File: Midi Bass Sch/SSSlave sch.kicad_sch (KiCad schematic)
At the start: 4 parts

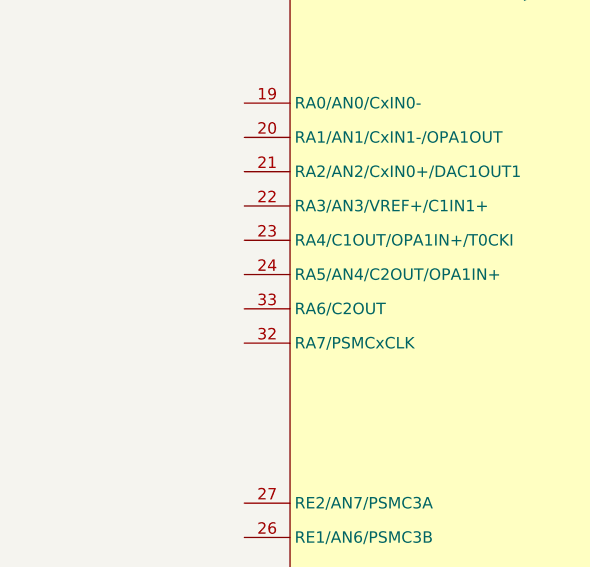
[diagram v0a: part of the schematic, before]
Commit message: updated schematic to include test points for pics
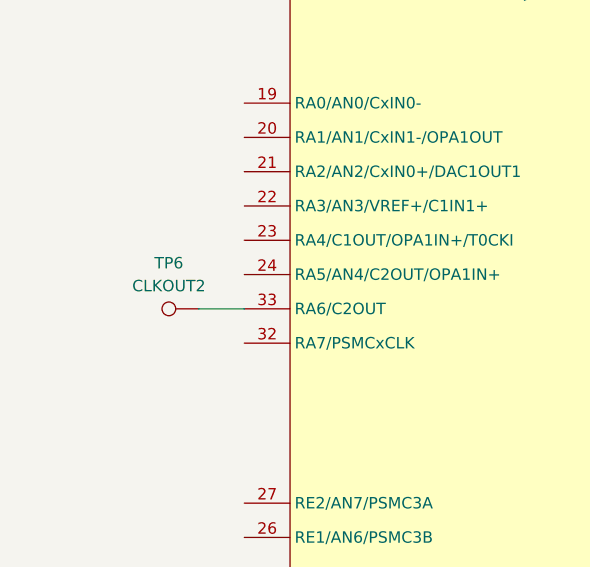
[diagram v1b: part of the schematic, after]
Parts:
- added TP6: CLKOUT2, symbol Connector:TestPoint
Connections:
- net at U3.33 (RA6/C2OUT): now also TP6.1
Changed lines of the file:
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@@
+	(wire
+		(pts
+			(xy 71.12 72.39) (xy 76.2 72.39)
+		)
+		(stroke
+			(width 0)
+			(type default)
+		)
+	)
 	(wire
 		(pts
@@
 					(unit 1)
 				)
+			)
+		)
+	)
+	(symbol
+		(lib_id "Connector:TestPoint")
+		(at 71.12 72.39 90)
+		(unit 1)
+		(exclude_from_sim no)
+		(in_bom yes)
+		(on_board yes)
+		(dnp no)
+		(fields_autoplaced yes)
+		(property "Reference" "TP6"
+			(at 67.818 67.31 90)
+			(effects
+				(font
+					(size 1.27 1.27)
+				)
+			)
+		)
+		(property "Value" "CLKOUT2"
+			(at 67.818 69.85 90)
+			(effects
+				(font
+					(size 1.27 1.27)
+				)
+			)
+		)
+		(property "Footprint" ""
+			(at 71.12 67.31 0)
+			(effects
+				(font
+					(size 1.27 1.27)
+				)
+				(hide yes)
+			)
+		)
+		(property "Datasheet" "~"
+			(at 71.12 67.31 0)
+			(effects
+				(font
+					(size 1.27 1.27)
+				)
+				(hide yes)
+			)
+		)
+		(property "Description" "test point"
+			(at 71.12 72.39 0)
+			(effects
+				(font
+					(size 1.27 1.27)
+				)
+				(hide yes)
+			)
+		)
+		(pin "1"
+		)
+		(instances
+			(project "Midi Bass Sch"
+				(path "/06818073-fb22-48ee-acc5-6dedd827034e/673444b1-2638-4f61-b545-e7cdf999c0e0"
+					(reference "TP6")
+					(unit 1)
+				)

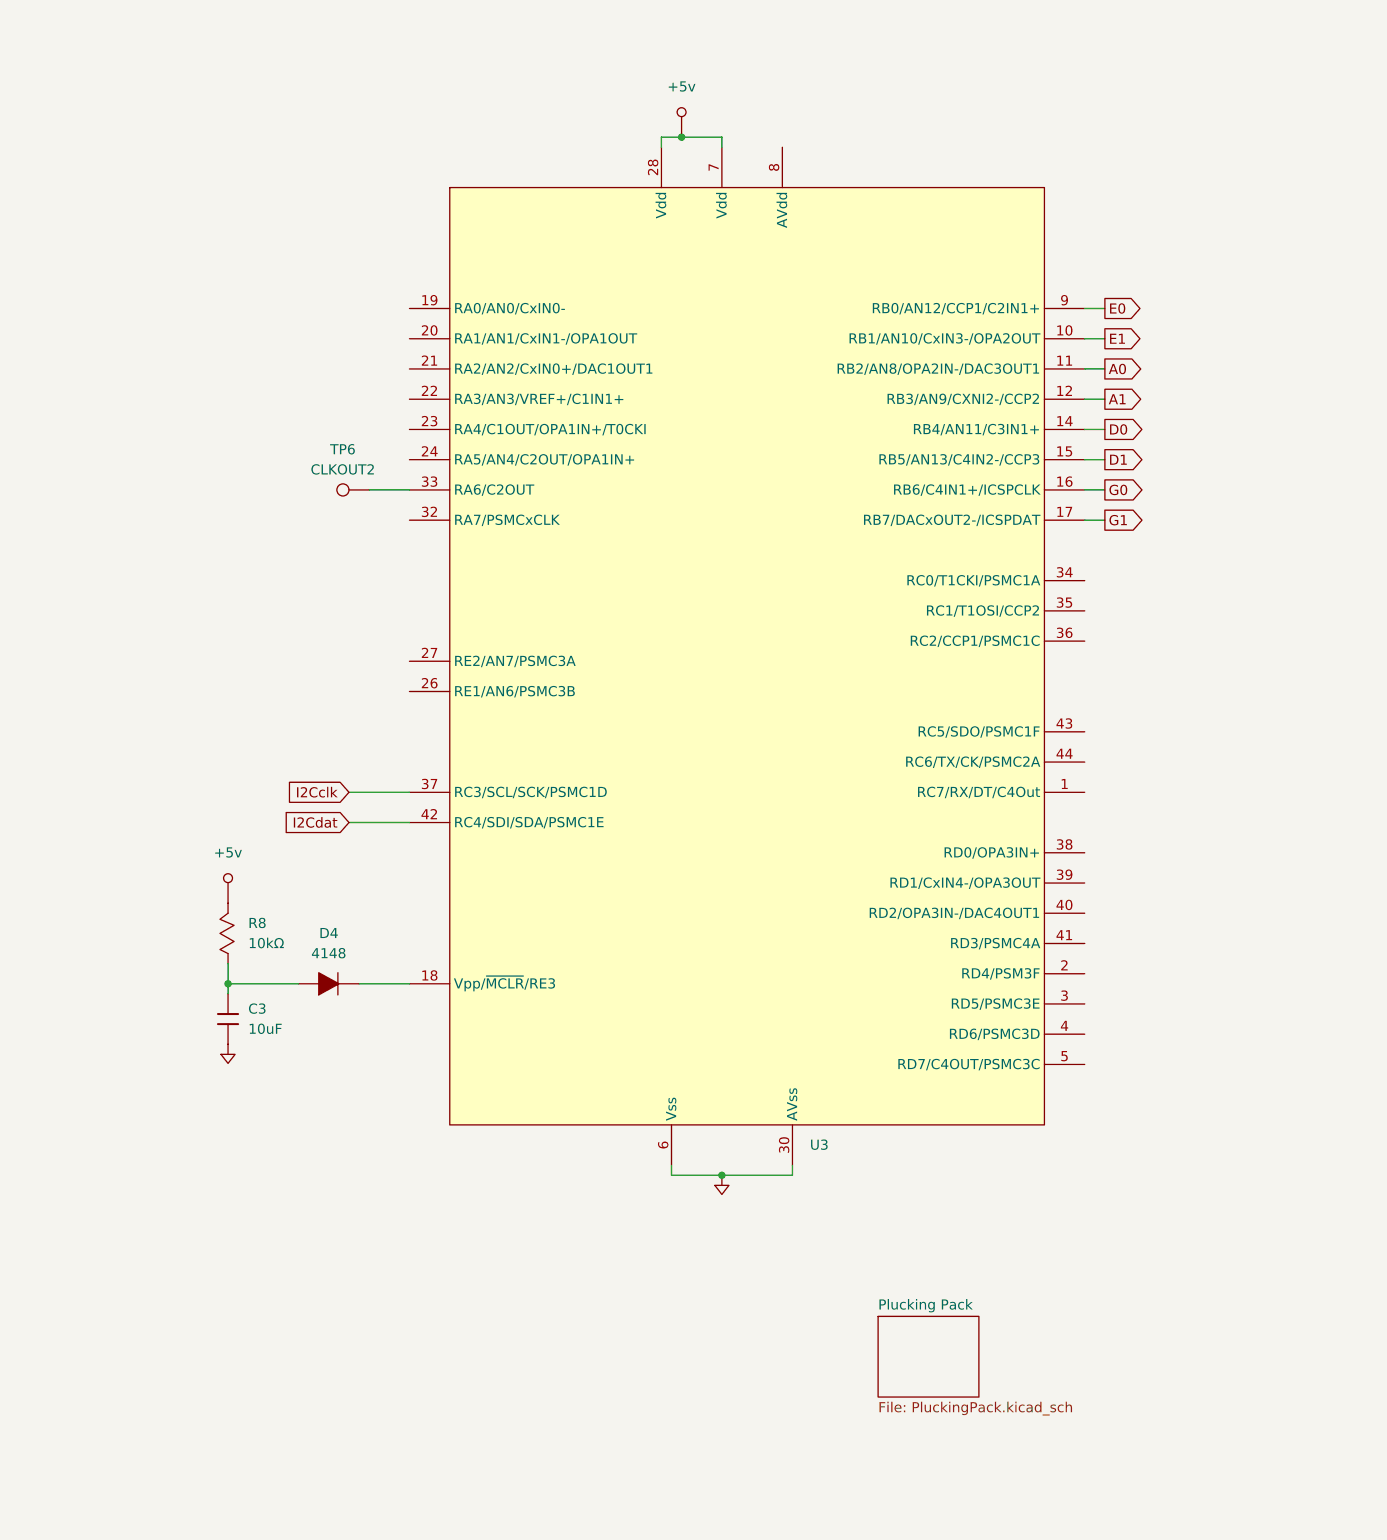
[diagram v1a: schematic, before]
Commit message: added solenoid array for the A slave
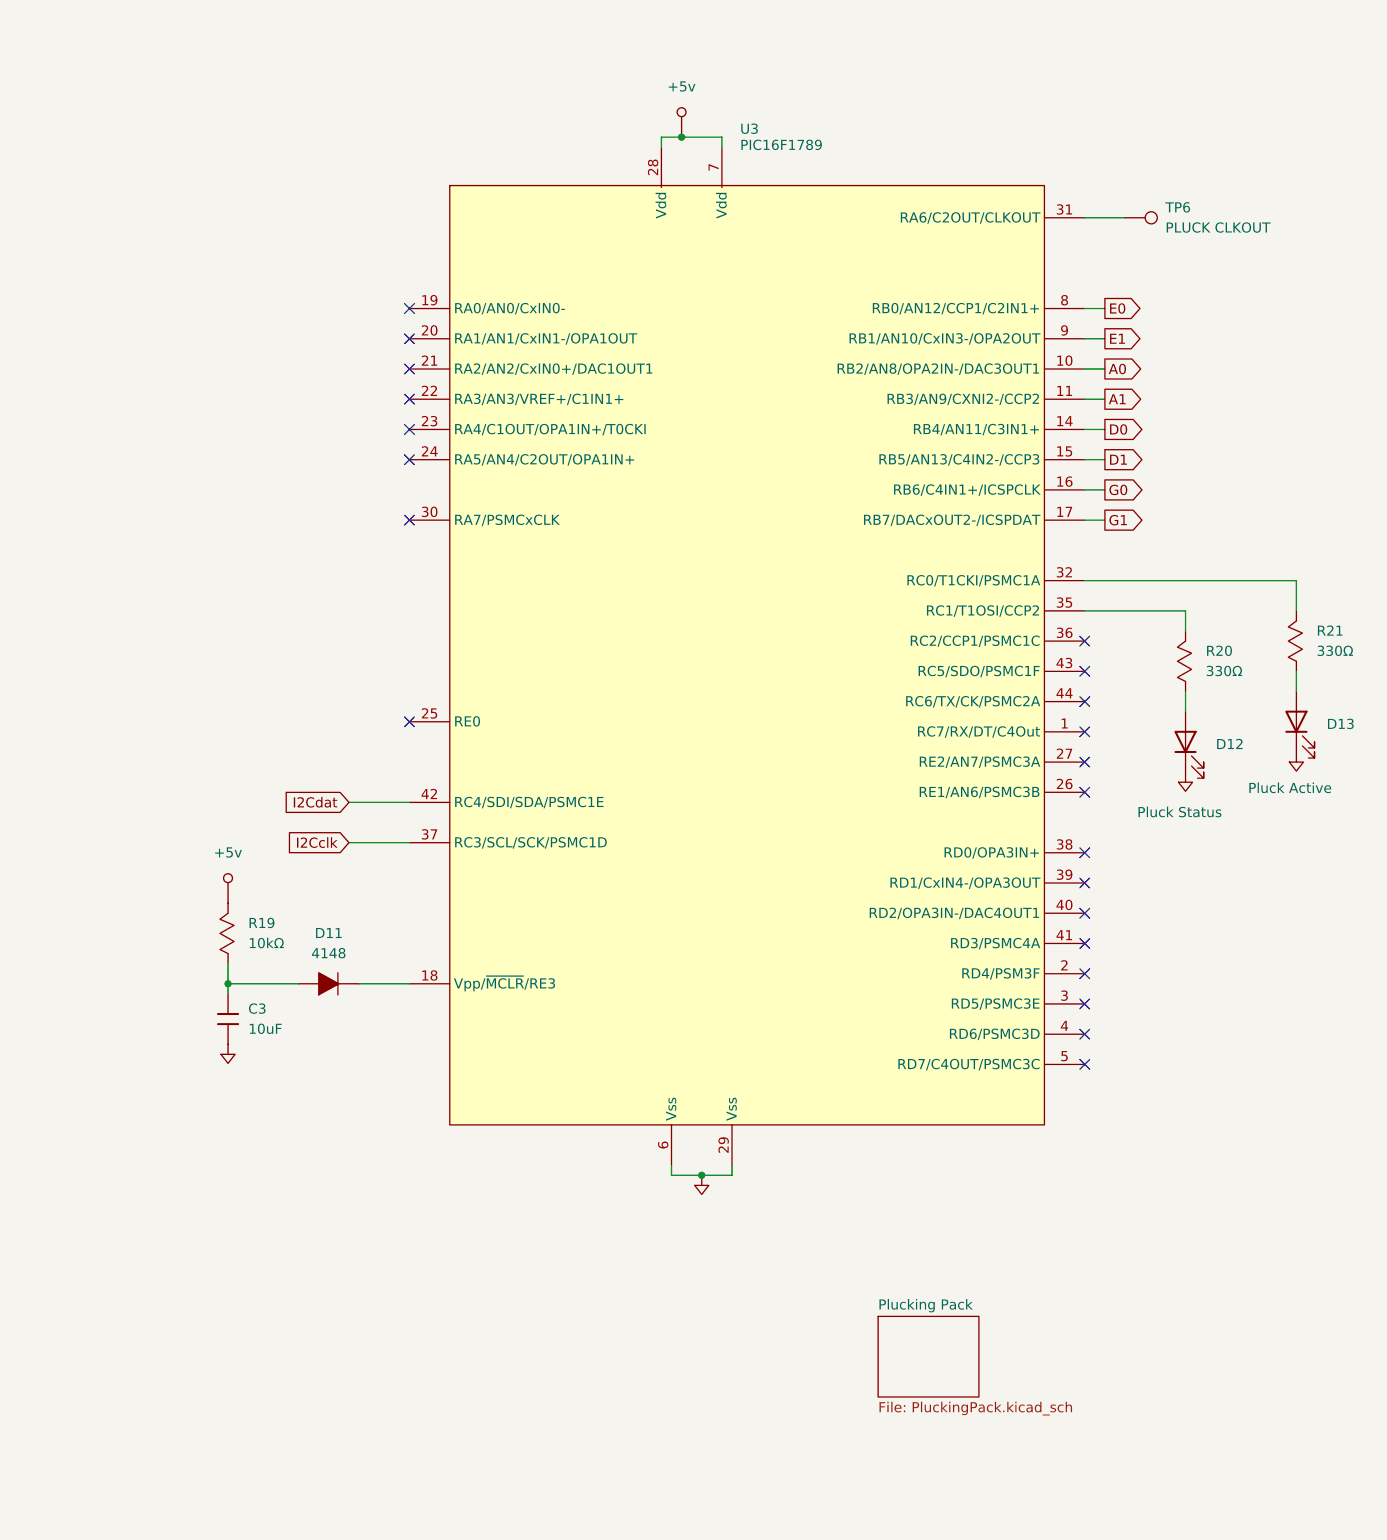
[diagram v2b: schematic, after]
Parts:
- added D12: Pluck Status, symbol Device:LED
- added D13: Pluck Active, symbol Device:LED
- added R20, R21: 330Ω, symbol Owen's Symbols:Resistor_Mod
- TP6: value CLKOUT2 -> PLUCK CLKOUT
- U3: value ~ -> PIC16F1789
- renumbered D4 to D11, R8 to R19
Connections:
- net A0: now also U3.10 (RB2/AN8/OPA2IN-/DAC3OUT1); no longer U3.11 (RB2/AN8/OPA2IN-/DAC3OUT1)
- net A1: now also U3.11 (RB3/AN9/CXNI2-/CCP2); no longer U3.12 (RB3/AN9/CXNI2-/CCP2)
- net E0: now also U3.8 (RB0/AN12/CCP1/C2IN1+); no longer U3.9 (RB0/AN12/CCP1/C2IN1+)
- net E1: now also U3.9 (RB1/AN10/CxIN3-/OPA2OUT); no longer U3.10 (RB1/AN10/CxIN3-/OPA2OUT)
- net GND: now also U3.29 (Vss), D12.1 (K), D13.1 (K); no longer U3.30 (AVss)
- net at TP6.1: now also U3.31 (RA6/C2OUT/CLKOUT); no longer U3.33 (RA6/C2OUT)
- net at U3.32 (RC0/T1CKI/PSMC1A): now also R21.2
- net at U3.35 (RC1/T1OSI/CCP2): now also R20.2
- new net: D13.2 (A), R21.1
- new net: D12.2 (A), R20.1
- no-connect marks 0 -> 22
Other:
- moved on the sheet: TP6

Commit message: added program pins to all processors
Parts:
- added J?: A SLAVE ISCP, symbol Owen's Symbols:Header_1x6
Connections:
- net +5v: now also J?.2
- net G0: now also J?.5
- net G1: now also J?.4
- net GND: now also J?.3
- net MSCLR P: now reaches D11.2, U3.18 (Vpp/~{MCLR}/RE3)
- net MSCLR P: now also J?.1
- no-connect marks 22 -> 23

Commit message: added footprints to kicad schematic still need footprint for din connector
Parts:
- C3: footprint (none) -> Capacitor_SMD:C_0805_2012Metric_Pad1.18x1.45mm_HandSolder
- D11, D12, D13: footprint (none) -> Diode_SMD:D_0805_2012Metric_Pad1.15x1.40mm_HandSolder
- J?: footprint (none) -> Connector_PinHeader_2.54mm:PinHeader_1x06_P2.54mm_Vertical
- R19, R20, R21: footprint (none) -> Resistor_SMD:R_0805_2012Metric_Pad1.20x1.40mm_HandSolder
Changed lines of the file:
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@@
 			)
 		)
-		(property "Footprint" ""
+		(property "Footprint" "Connector_PinHeader_2.54mm:PinHeader_1x06_P2.54mm_Vertical"
 			(at 34.29 62.23 0)
 			(effects
@@
 			)
 		)
-		(property "Footprint" ""
+		(property "Footprint" "Resistor_SMD:R_0805_2012Metric_Pad1.20x1.40mm_HandSolder"
 			(at 185.42 92.71 0)
 			(effects
@@
 			)
 		)
-		(property "Footprint" ""
+		(property "Footprint" "Diode_SMD:D_0805_2012Metric_Pad1.15x1.40mm_HandSolder"
 			(at 187.96 101.6 0)
 			(effects
@@
 			)
 		)
-		(property "Footprint" ""
+		(property "Footprint" "Resistor_SMD:R_0805_2012Metric_Pad1.20x1.40mm_HandSolder"
 			(at 171.45 95.25 0)
 			(effects
@@
 			)
 		)
-		(property "Footprint" ""
+		(property "Footprint" "Resistor_SMD:R_0805_2012Metric_Pad1.20x1.40mm_HandSolder"
 			(at 50.8 129.54 0)
 			(effects
@@
 			)
 		)
-		(property "Footprint" ""
+		(property "Footprint" "Diode_SMD:D_0805_2012Metric_Pad1.15x1.40mm_HandSolder"
 			(at 62.23 134.62 0)
 			(effects
@@
 			)
 		)
-		(property "Footprint" ""
+		(property "Footprint" "Capacitor_SMD:C_0805_2012Metric_Pad1.18x1.45mm_HandSolder"
 			(at 53.34 133.35 0)
 			(effects
@@
 			)
 		)
-		(property "Footprint" ""
+		(property "Footprint" "Diode_SMD:D_0805_2012Metric_Pad1.15x1.40mm_HandSolder"
 			(at 173.99 104.14 0)
 			(effects

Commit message: started basic pcb layout for Master pic
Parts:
- gave numbers to parts that had none: 1
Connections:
- net MSCLR P: now also D11.1; no longer D11.2
- net at C3.1, R19.1: now also D11.2; no longer D11.1
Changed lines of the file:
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@@
 		(dnp no)
 		(fields_autoplaced yes)
-		(property "Reference" "#PWR032"
+		(property "Reference" "#PWR034"
 			(at 53.34 140.97 0)
 			(effects
@@
 			(project "Midi Bass Sch"
 				(path "/06818073-fb22-48ee-acc5-6dedd827034e/673444b1-2638-4f61-b545-e7cdf999c0e0"
-					(reference "#PWR032")
+					(reference "#PWR034")
 					(unit 1)
 				)
@@
 		(dnp no)
 		(fields_autoplaced yes)
-		(property "Reference" "#PWR036"
+		(property "Reference" "#PWR038"
 			(at 187.96 104.14 0)
 			(effects
@@
 			(project "Midi Bass Sch"
 				(path "/06818073-fb22-48ee-acc5-6dedd827034e/673444b1-2638-4f61-b545-e7cdf999c0e0"
-					(reference "#PWR036")
+					(reference "#PWR038")
 					(unit 1)
 				)
@@
 		(dnp no)
 		(fields_autoplaced yes)
-		(property "Reference" "J?"
+		(property "Reference" "J4"
 			(at 34.29 58.42 0)
 			(effects
@@
 			(project "Midi Bass Sch"
 				(path "/06818073-fb22-48ee-acc5-6dedd827034e/673444b1-2638-4f61-b545-e7cdf999c0e0"
-					(reference "J?")
+					(reference "J4")
 					(unit 1)
 				)
@@
 		(dnp no)
 		(fields_autoplaced yes)
-		(property "Reference" "#PWR031"
+		(property "Reference" "#PWR033"
 			(at 58.0644 119.4816 0)
 			(effects
@@
 			(project "Midi Bass Sch"
 				(path "/06818073-fb22-48ee-acc5-6dedd827034e/673444b1-2638-4f61-b545-e7cdf999c0e0"
-					(reference "#PWR031")
+					(reference "#PWR033")
 					(unit 1)
 				)
@@
 		(dnp no)
 		(fields_autoplaced yes)
-		(property "Reference" "#PWR034"
+		(property "Reference" "#PWR036"
 			(at 113.03 157.48 0)
 			(effects
@@
 			(project "Midi Bass Sch"
 				(path "/06818073-fb22-48ee-acc5-6dedd827034e/673444b1-2638-4f61-b545-e7cdf999c0e0"
-					(reference "#PWR034")
+					(reference "#PWR036")
 					(unit 1)
 				)
@@
 		(dnp no)
 		(fields_autoplaced yes)
-		(property "Reference" "#PWR033"
+		(property "Reference" "#PWR035"
 			(at 115.2144 22.9616 0)
 			(effects
@@
 			(project "Midi Bass Sch"
 				(path "/06818073-fb22-48ee-acc5-6dedd827034e/673444b1-2638-4f61-b545-e7cdf999c0e0"
-					(reference "#PWR033")
+					(reference "#PWR035")
 					(unit 1)
 				)
@@
 		(dnp no)
 		(fields_autoplaced yes)
-		(property "Reference" "#PWR0329"
+		(property "Reference" "#PWR032"
 			(at 45.72 71.12 0)
 			(effects
@@
 			(project "Midi Bass Sch"
 				(path "/06818073-fb22-48ee-acc5-6dedd827034e/673444b1-2638-4f61-b545-e7cdf999c0e0"
-					(reference "#PWR0329")
+					(reference "#PWR032")
 					(unit 1)
 				)
@@
 		(dnp no)
 		(fields_autoplaced yes)
-		(property "Reference" "#PWR035"
+		(property "Reference" "#PWR037"
 			(at 173.99 106.68 0)
 			(effects
@@
 			(project "Midi Bass Sch"
 				(path "/06818073-fb22-48ee-acc5-6dedd827034e/673444b1-2638-4f61-b545-e7cdf999c0e0"
-					(reference "#PWR035")
+					(reference "#PWR037")
 					(unit 1)
 				)
@@
 		(dnp no)
 		(fields_autoplaced yes)
-		(property "Reference" "#PWR0328"
+		(property "Reference" "#PWR031"
 			(at 50.4444 58.5216 0)
 			(effects
@@
 			(project "Midi Bass Sch"
 				(path "/06818073-fb22-48ee-acc5-6dedd827034e/673444b1-2638-4f61-b545-e7cdf999c0e0"
-					(reference "#PWR0328")
-					(unit 1)
-				)
+					(reference "#PWR031")
+					(unit 1)
+				)

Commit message: began adding mute application to plucking unit
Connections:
- net E MUTE: now reaches U3.38 (RD0/OPA3IN+)
- net A MUTE: now reaches U3.39 (RD1/CxIN4-/OPA3OUT)
- net D MUTE: now reaches U3.40 (RD2/OPA3IN-/DAC4OUT1)
- net G MUTE: now reaches U3.41 (RD3/PSMC4A)
- no-connect marks 23 -> 19
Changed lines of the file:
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@@
-	)
-	(no_connect
-		(at 161.29 125.73)
 	)
 	(no_connect
@@
 	)
 	(no_connect
-		(at 161.29 129.54)
-	)
-	(no_connect
 		(at 76.2 57.15)
 	)
@@
 	)
 	(no_connect
-		(at 161.29 118.11)
-	)
-	(no_connect
 		(at 38.1 78.74)
 	)
@@
 	)
 	(no_connect
-		(at 161.29 121.92)
-	)
-	(no_connect
 		(at 161.29 106.68)
 	)
@@
 	(wire
 		(pts
+			(xy 161.29 125.73) (xy 165.1 125.73)
+		)
+		(stroke
+			(width 0)
+			(type default)
+		)
+	)
+	(wire
+		(pts
 			(xy 115.57 27.94) (xy 115.57 29.21)
 		)
@@
 	(wire
 		(pts
+			(xy 161.29 129.54) (xy 165.1 129.54)
+		)
+		(stroke
+			(width 0)
+			(type default)
+		)
+	)
+	(wire
+		(pts
 			(xy 107.95 27.94) (xy 110.49 27.94)
 		)
@@
 	(wire
 		(pts
+			(xy 161.29 118.11) (xy 165.1 118.11)
+		)
+		(stroke
+			(width 0)
+			(type default)
+		)
+	)
+	(wire
+		(pts
 			(xy 41.91 81.28) (xy 41.91 76.2)
 		)
@@
 		(pts
 			(xy 162.56 77.47) (xy 162.56 76.2)
+		)
+		(stroke
+			(width 0)
+			(type default)
+		)
+	)
+	(wire
+		(pts
+			(xy 161.29 121.92) (xy 165.1 121.92)
 		)
 		(stroke
@@
 		)
 	)
+	(global_label "A MUTE"
+		(shape output)
+		(at 165.1 121.92 0)
+		(fields_autoplaced yes)
+		(effects
+			(font
+				(size 1.27 1.27)
+			)
+			(justify left)
+		)
+		(property "Intersheetrefs" "${INTERSHEET_REFS}"
+			(at 175.0399 121.92 0)
+			(effects
+				(font
+					(size 1.27 1.27)
+				)
+				(justify left)
+				(hide yes)
+			)
+		)
+	)
 	(global_label "I2Cclk"
 		(shape input)
@@
 		)
 	)
+	(global_label "D MUTE"
+		(shape output)
+		(at 165.1 125.73 0)
+		(fields_autoplaced yes)
+		(effects
+			(font
+				(size 1.27 1.27)
+			)
+			(justify left)
+		)
+		(property "Intersheetrefs" "${INTERSHEET_REFS}"
+			(at 175.2213 125.73 0)
+			(effects
+				(font
+					(size 1.27 1.27)
+				)
+				(justify left)
+				(hide yes)
+			)
+		)
+	)
+	(global_label "E MUTE"
+		(shape output)
+		(at 165.1 118.11 0)
+		(fields_autoplaced yes)
+		(effects
+			(font
+				(size 1.27 1.27)
+			)
+			(justify left)
+		)
+		(property "Intersheetrefs" "${INTERSHEET_REFS}"
+			(at 175.1003 118.11 0)
+			(effects
+				(font
+					(size 1.27 1.27)
+				)
+				(justify left)
+				(hide yes)
+			)
+		)
+	)
 	(global_label "RB7 P"
 		(shape passive)
@@
 				(hide yes)
 			)
+		)
+	)
+	(global_label "G MUTE"
+		(shape output)
+		(at 165.1 129.54 0)
+		(fields_autoplaced yes)
+		(effects
+			(font
+				(size 1.27 1.27)
+			)
+			(justify left)
+		)
+		(property "Intersheetrefs" "${INTERSHEET_REFS}"
+			(at 175.2213 129.54 0)
+			(effects
+				(font
+					(size 1.27 1.27)
+				)
+				(justify left)
+				(hide yes)
+			)
